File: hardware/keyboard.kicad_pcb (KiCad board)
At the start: 2 copper layers, 64 parts

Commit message: Progress on circuit design
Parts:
- moved CHERRY 350.5 mm to (0.00, 0.00)
- moved CHERRY 148.0 mm to (154.5, 211.2)
- moved CHERRY 117.4 mm to (96.8, -56.9)
- moved CHERRY 117.4 mm to (115.8, -56.6)
- moved CHERRY 117.4 mm to (331.0, 17.0)
- moved CHERRY 117.4 mm to (342.4, -40.1)
- moved CHERRY 117.4 mm to (298.7, -56.9)
- moved CHERRY 117.4 mm to (289.6, -1.02)
- moved CHERRY 117.4 mm to (283.0, -38.1)
- moved CHERRY 117.4 mm to (75.4, -58.4)
- moved CHERRY 117.4 mm to (345.7, -21.6)
- moved CHERRY 117.4 mm to (327.7, -1.52)
- moved CHERRY 117.4 mm to (324.4, -20.1)
- moved CHERRY 117.4 mm to (317.8, -57.1)
- moved CHERRY 117.4 mm to (308.6, -1.27)
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
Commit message: WIP schematic + PCB design
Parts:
- removed CHERRY (x10): MX, keyboard-modules:CHERRY_PCB_125H
- removed CHERRY (x4): MX, keyboard-modules:CHERRY_PCB_150H
- removed CHERRY (x50): MX, keyboard-modules:CHERRY_PCB_100H
- added C1: 18pF, Capacitors_SMD:C_1206_HandSoldering, F.Cu at (273.9, 52.7)
- added C2: 18pF, Capacitors_SMD:C_1206_HandSoldering, F.Cu at (253.1, 58.5)
- added C3: 1uF, Capacitors_SMD:C_1206_HandSoldering, F.Cu at (260.0, 58.5)
- added D1: LED, LEDs:LED_1206, F.Cu at (401.9, 52.6)
- added D10: D_Small, Diodes_SMD:D_1206, F.Cu at (381.9, 58.5)
- added D11: D_Small, Diodes_SMD:D_1206, F.Cu at (183.9, 83.3)
- added D12: D_Small, Diodes_SMD:D_1206, F.Cu at (190.3, 77.6)
- added D13: D_Small, Diodes_SMD:D_1206, F.Cu at (389.4, 52.8)
- added D14: D_Small, Diodes_SMD:D_1206, F.Cu at (203.2, 45.9)
- added D15: D_Small, Diodes_SMD:D_1206, F.Cu at (203.2, 40.2)
- added D16: D_Small, Diodes_SMD:D_1206, F.Cu at (375.5, 58.5)
- added D17: D_Small, Diodes_SMD:D_1206, F.Cu at (369.1, 58.5)
- added D18: D_Small, Diodes_SMD:D_1206, F.Cu at (203.2, 57.4)
- added D19: D_Small, Diodes_SMD:D_1206, F.Cu at (209.6, 51.7)
- added D2: D_Small, Diodes_SMD:D_1206, F.Cu at (196.7, 77.6)
- added D20: D_Small, Diodes_SMD:D_1206, F.Cu at (203.2, 51.7)
- added D21: D_Small, Diodes_SMD:D_1206, F.Cu at (209.6, 45.9)
- added D22: D_Small, Diodes_SMD:D_1206, F.Cu at (349.9, 58.5)
- added D23: D_Small, Diodes_SMD:D_1206, F.Cu at (209.6, 40.2)
- added D24: D_Small, Diodes_SMD:D_1206, F.Cu at (376.6, 52.8)
- added D25: D_Small, Diodes_SMD:D_1206, F.Cu at (209.6, 34.4)
- added D26: D_Small, Diodes_SMD:D_1206, F.Cu at (362.7, 58.5)
- added D27: D_Small, Diodes_SMD:D_1206, F.Cu at (370.2, 52.8)
- added D28: D_Small, Diodes_SMD:D_1206, F.Cu at (363.8, 52.8)
- added D29: D_Small, Diodes_SMD:D_1206, F.Cu at (357.4, 52.8)
- added D3: D_Small, Diodes_SMD:D_1206, F.Cu at (190.3, 83.3)
- added D30: D_Small, Diodes_SMD:D_1206, F.Cu at (356.3, 58.5)
- added D31: D_Small, Diodes_SMD:D_1206, F.Cu at (183.9, 94.8)
- added D32: D_Small, Diodes_SMD:D_1206, F.Cu at (383.0, 52.8)
- added D33: D_Small, Diodes_SMD:D_1206, F.Cu at (183.9, 89.1)
- added D34: D_Small, Diodes_SMD:D_1206, F.Cu at (209.6, 28.7)
- added D35: D_Small, Diodes_SMD:D_1206, F.Cu at (203.2, 28.7)
- added D36: D_Small, Diodes_SMD:D_1206, F.Cu at (209.6, 22.9)
- added D37: D_Small, Diodes_SMD:D_1206, F.Cu at (203.2, 22.9)
- added D38: D_Small, Diodes_SMD:D_1206, F.Cu at (209.6, 17.2)
- added D39: D_Small, Diodes_SMD:D_1206, F.Cu at (343.5, 58.5)
- added D4: D_Small, Diodes_SMD:D_1206, F.Cu at (388.3, 58.5)
- added D40: D_Small, Diodes_SMD:D_1206, F.Cu at (319.0, 52.8)
- added D41: D_Small, Diodes_SMD:D_1206, F.Cu at (337.1, 58.5)
- added D42: D_Small, Diodes_SMD:D_1206, F.Cu at (203.2, 34.4)
- added D43: D_Small, Diodes_SMD:D_1206, F.Cu at (344.6, 52.8)
- added D44: D_Small, Diodes_SMD:D_1206, F.Cu at (203.2, 17.2)
- added D45: D_Small, Diodes_SMD:D_1206, F.Cu at (338.2, 52.8)
- added D46: D_Small, Diodes_SMD:D_1206, F.Cu at (330.7, 58.5)
- added D47: D_Small, Diodes_SMD:D_1206, F.Cu at (324.3, 58.5)
- added D48: D_Small, Diodes_SMD:D_1206, F.Cu at (331.8, 52.8)
- added D49: D_Small, Diodes_SMD:D_1206, F.Cu at (325.4, 52.8)
- added D5: D_Small, Diodes_SMD:D_1206, F.Cu at (203.2, 68.9)
- added D50: D_Small, Diodes_SMD:D_1206, F.Cu at (285.9, 58.5)
- added D51: D_Small, Diodes_SMD:D_1206, F.Cu at (317.9, 58.5)
- added D52: D_Small, Diodes_SMD:D_1206, F.Cu at (311.5, 58.5)
- added D53: D_Small, Diodes_SMD:D_1206, F.Cu at (305.1, 58.5)
- added D54: D_Small, Diodes_SMD:D_1206, F.Cu at (312.6, 52.8)
- added D55: D_Small, Diodes_SMD:D_1206, F.Cu at (306.2, 52.8)
- added D56: D_Small, Diodes_SMD:D_1206, F.Cu at (299.8, 52.8)
- added D57: D_Small, Diodes_SMD:D_1206, F.Cu at (298.7, 58.5)
- added D58: D_Small, Diodes_SMD:D_1206, F.Cu at (292.3, 58.5)
- added D59: D_Small, Diodes_SMD:D_1206, F.Cu at (183.9, 77.6)
- added D6: D_Small, Diodes_SMD:D_1206, F.Cu at (209.6, 63.2)
- added D60: D_Small, Diodes_SMD:D_1206, F.Cu at (293.4, 52.8)
- added D61: D_Small, Diodes_SMD:D_1206, F.Cu at (287.0, 52.8)
- added D62: D_Small, Diodes_SMD:D_1206, F.Cu at (280.6, 52.8)
- added D63: D_Small, Diodes_SMD:D_1206, F.Cu at (279.5, 58.6)
- added D64: D_Small, Diodes_SMD:D_1206, F.Cu at (273.1, 58.6)
- added D65: D_Small, Diodes_SMD:D_1206, F.Cu at (266.7, 58.6)
- added D66: D_Small, Diodes_SMD:D_1206, F.Cu at (351.0, 52.8)
- added D7: D_Small, Diodes_SMD:D_1206, F.Cu at (395.8, 52.8)
- added D8: D_Small, Diodes_SMD:D_1206, F.Cu at (203.2, 63.2)
- added D9: D_Small, Diodes_SMD:D_1206, F.Cu at (209.6, 57.4)
- added F1: Polyfuse_Small, Fuse_Holders_and_Fuses:Fuse_SMD1206_HandSoldering, F.Cu at (234.6, 53.2)
- added J1: USB_OTG, Connectors_USB:USB_Micro-B_Molex-105017-0001, F.Cu at (245.0, 55.0)
- added R1: 1k, Resistors_SMD:R_1206_HandSoldering, F.Cu at (267.0, 52.8)
- added R2: 22, Resistors_SMD:R_1206_HandSoldering, F.Cu at (260.0, 52.8)
- added R3: 22, Resistors_SMD:R_1206_HandSoldering, F.Cu at (253.1, 52.8)
- added S1: SPST, keyboard-modules:CHERRY_PCB_100H, F.Cu at (362.9, 118.5)
- added S10: SPST, keyboard-modules:CHERRY_PCB_100H, F.Cu at (304.9, 118.5)
- added S11: SPST, keyboard-modules:CHERRY_PCB_100H, F.Cu at (324.2, 137.9)
- added S12: SPST, keyboard-modules:CHERRY_PCB_100H, F.Cu at (285.6, 137.9)
- added S13: SPST, keyboard-modules:CHERRY_PCB_100H, F.Cu at (362.9, 176.5)
- added S14: SPST, keyboard-modules:CHERRY_PCB_100H, F.Cu at (141.6, 120.0)
- added S15: SPST, keyboard-modules:CHERRY_PCB_100H, F.Cu at (266.2, 176.5)
- added S16: SPST, keyboard-modules:CHERRY_PCB_100H, F.Cu at (186.2, 214.8)
- added S17: SPST, keyboard-modules:CHERRY_PCB_100H, F.Cu at (285.6, 118.5)
- added S18: SPST, keyboard-modules:CHERRY_PCB_100H, F.Cu at (304.9, 137.9)
- added S19: SPST, keyboard-modules:CHERRY_PCB_100H, F.Cu at (324.2, 157.2)
- added S2: SPST, keyboard-modules:CHERRY_PCB_100H, F.Cu at (244.2, 214.8)
- added S20: SPST, keyboard-modules:CHERRY_PCB_100H, F.Cu at (343.6, 176.5)
- added S21: SPST, keyboard-modules:CHERRY_PCB_100H, F.Cu at (362.9, 195.9)
- added S22: SPST, keyboard-modules:CHERRY_PCB_100H, F.Cu at (266.2, 118.5)
- added S23: SPST, keyboard-modules:CHERRY_PCB_100H, F.Cu at (64.3, 139.3)
- added S24: SPST, keyboard-modules:CHERRY_PCB_100H, F.Cu at (304.9, 157.2)
- added S25: SPST, keyboard-modules:CHERRY_PCB_100H, F.Cu at (324.2, 176.5)
- added S26: SPST, keyboard-modules:CHERRY_PCB_100H, F.Cu at (343.6, 195.9)
- added S27: SPST, keyboard-modules:CHERRY_PCB_100H, F.Cu at (161.0, 120.0)
- added S28: SPST, keyboard-modules:CHERRY_PCB_100H, F.Cu at (266.2, 137.9)
- added S29: SPST, keyboard-modules:CHERRY_PCB_100H, F.Cu at (285.6, 157.2)
- added S3: SPST, keyboard-modules:CHERRY_PCB_100H, F.Cu at (362.9, 137.9)
- added S30: SPST, keyboard-modules:CHERRY_PCB_100H, F.Cu at (304.9, 176.5)
- added S31: SPST, keyboard-modules:CHERRY_PCB_100H, F.Cu at (324.2, 195.9)
- added S32: SPST, keyboard-modules:CHERRY_PCB_100H, F.Cu at (324.2, 118.5)
- added S33: SPST, keyboard-modules:CHERRY_PCB_100H, F.Cu at (266.2, 157.2)
- added S34: SPST, keyboard-modules:CHERRY_PCB_100H, F.Cu at (285.6, 176.5)
- added S35: SPST, keyboard-modules:CHERRY_PCB_100H, F.Cu at (304.9, 195.9)
- added S36: SPST, keyboard-modules:CHERRY_PCB_100H, F.Cu at (122.3, 120.0)
- added S37: SPST, keyboard-modules:CHERRY_PCB_100H, F.Cu at (141.6, 139.3)
- added S38: SPST, keyboard-modules:CHERRY_PCB_100H, F.Cu at (161.0, 158.7)
- added S39: SPST, keyboard-modules:CHERRY_PCB_100H, F.Cu at (122.3, 158.7)
- added S4: SPST, keyboard-modules:CHERRY_PCB_100H, F.Cu at (343.6, 118.5)
- added S40: SPST, keyboard-modules:CHERRY_PCB_100H, F.Cu at (285.6, 195.9)
- added S41: SPST, keyboard-modules:CHERRY_PCB_100H, F.Cu at (161.0, 139.3)
- added S42: SPST, keyboard-modules:CHERRY_PCB_100H, F.Cu at (103.0, 120.0)
- added S43: SPST, keyboard-modules:CHERRY_PCB_100H, F.Cu at (122.3, 139.3)
- added S44: SPST, keyboard-modules:CHERRY_PCB_100H, F.Cu at (141.6, 158.7)
- added S45: SPST, keyboard-modules:CHERRY_PCB_100H, F.Cu at (161.0, 178.0)
- added S46: SPST, keyboard-modules:CHERRY_PCB_100H, F.Cu at (266.2, 195.9)
- added S47: SPST, keyboard-modules:CHERRY_PCB_100H, F.Cu at (83.6, 120.0)
- added S48: SPST, keyboard-modules:CHERRY_PCB_100H, F.Cu at (103.0, 139.3)
- added S49: SPST, keyboard-modules:CHERRY_PCB_100H, F.Cu at (103.0, 178.0)
- added S5: SPST, keyboard-modules:CHERRY_PCB_100H, F.Cu at (224.9, 214.8)
- added S50: SPST, keyboard-modules:CHERRY_PCB_100H, F.Cu at (161.0, 197.3)
- added S51: SPST, keyboard-modules:CHERRY_PCB_100H, F.Cu at (64.3, 120.0)
- added S52: SPST, keyboard-modules:CHERRY_PCB_100H, F.Cu at (83.6, 139.3)
- added S53: SPST, keyboard-modules:CHERRY_PCB_100H, F.Cu at (103.0, 158.7)
- added S54: SPST, keyboard-modules:CHERRY_PCB_100H, F.Cu at (122.3, 178.0)
- added S55: SPST, keyboard-modules:CHERRY_PCB_100H, F.Cu at (141.6, 197.3)
- added S56: SPST, keyboard-modules:CHERRY_PCB_100H, F.Cu at (64.3, 197.3)
- added S57: SPST, keyboard-modules:CHERRY_PCB_100H, F.Cu at (83.6, 158.7)
- added S58: SPST, keyboard-modules:CHERRY_PCB_100H, F.Cu at (141.6, 178.0)
- added S59: SPST, keyboard-modules:CHERRY_PCB_100H, F.Cu at (122.3, 197.3)
- added S6: SPST, keyboard-modules:CHERRY_PCB_100H, F.Cu at (343.6, 157.2)
- added S60: SPST, keyboard-modules:CHERRY_PCB_100H, F.Cu at (64.3, 158.7)
- added S61: SPST, keyboard-modules:CHERRY_PCB_100H, F.Cu at (83.6, 178.0)
- added S62: SPST, keyboard-modules:CHERRY_PCB_100H, F.Cu at (103.0, 197.3)
- added S63: SPST, keyboard-modules:CHERRY_PCB_100H, F.Cu at (64.3, 178.0)
- added S64: SPST, keyboard-modules:CHERRY_PCB_100H, F.Cu at (83.6, 197.3)
- added S7: SPST, keyboard-modules:CHERRY_PCB_100H, F.Cu at (343.6, 137.9)
- added S8: SPST, keyboard-modules:CHERRY_PCB_100H, F.Cu at (362.9, 157.2)
- added S9: SPST, keyboard-modules:CHERRY_PCB_100H, F.Cu at (205.5, 214.8)
- added U1: ATMEGA32U4-AU, Housings_QFP:TQFP-44_10x10mm_Pitch0.8mm, F.Cu at (207.0, 5.88)
- added Y1: 16MHz, Crystals:Crystal_SMD_2012-2pin_2.0x1.2mm_HandSoldering, F.Cu at (394.1, 58.5)

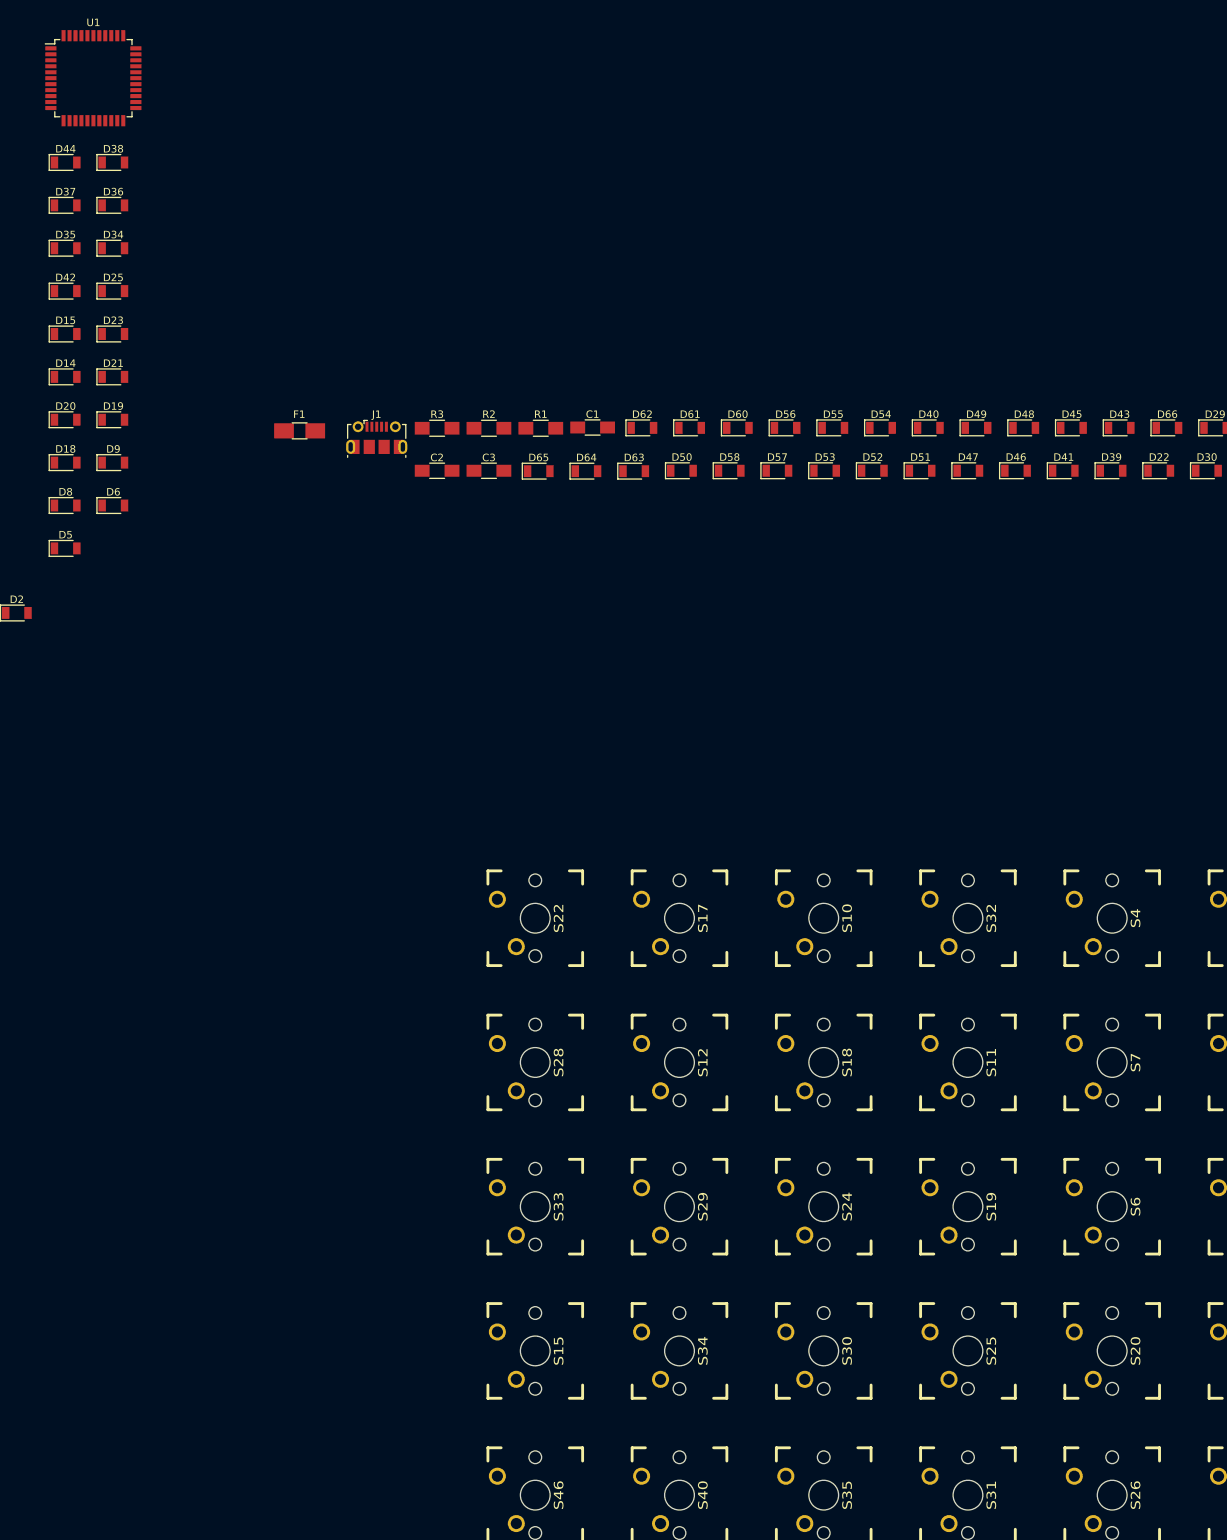
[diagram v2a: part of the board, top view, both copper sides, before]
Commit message: Extract keys into sheets, add MCP23018
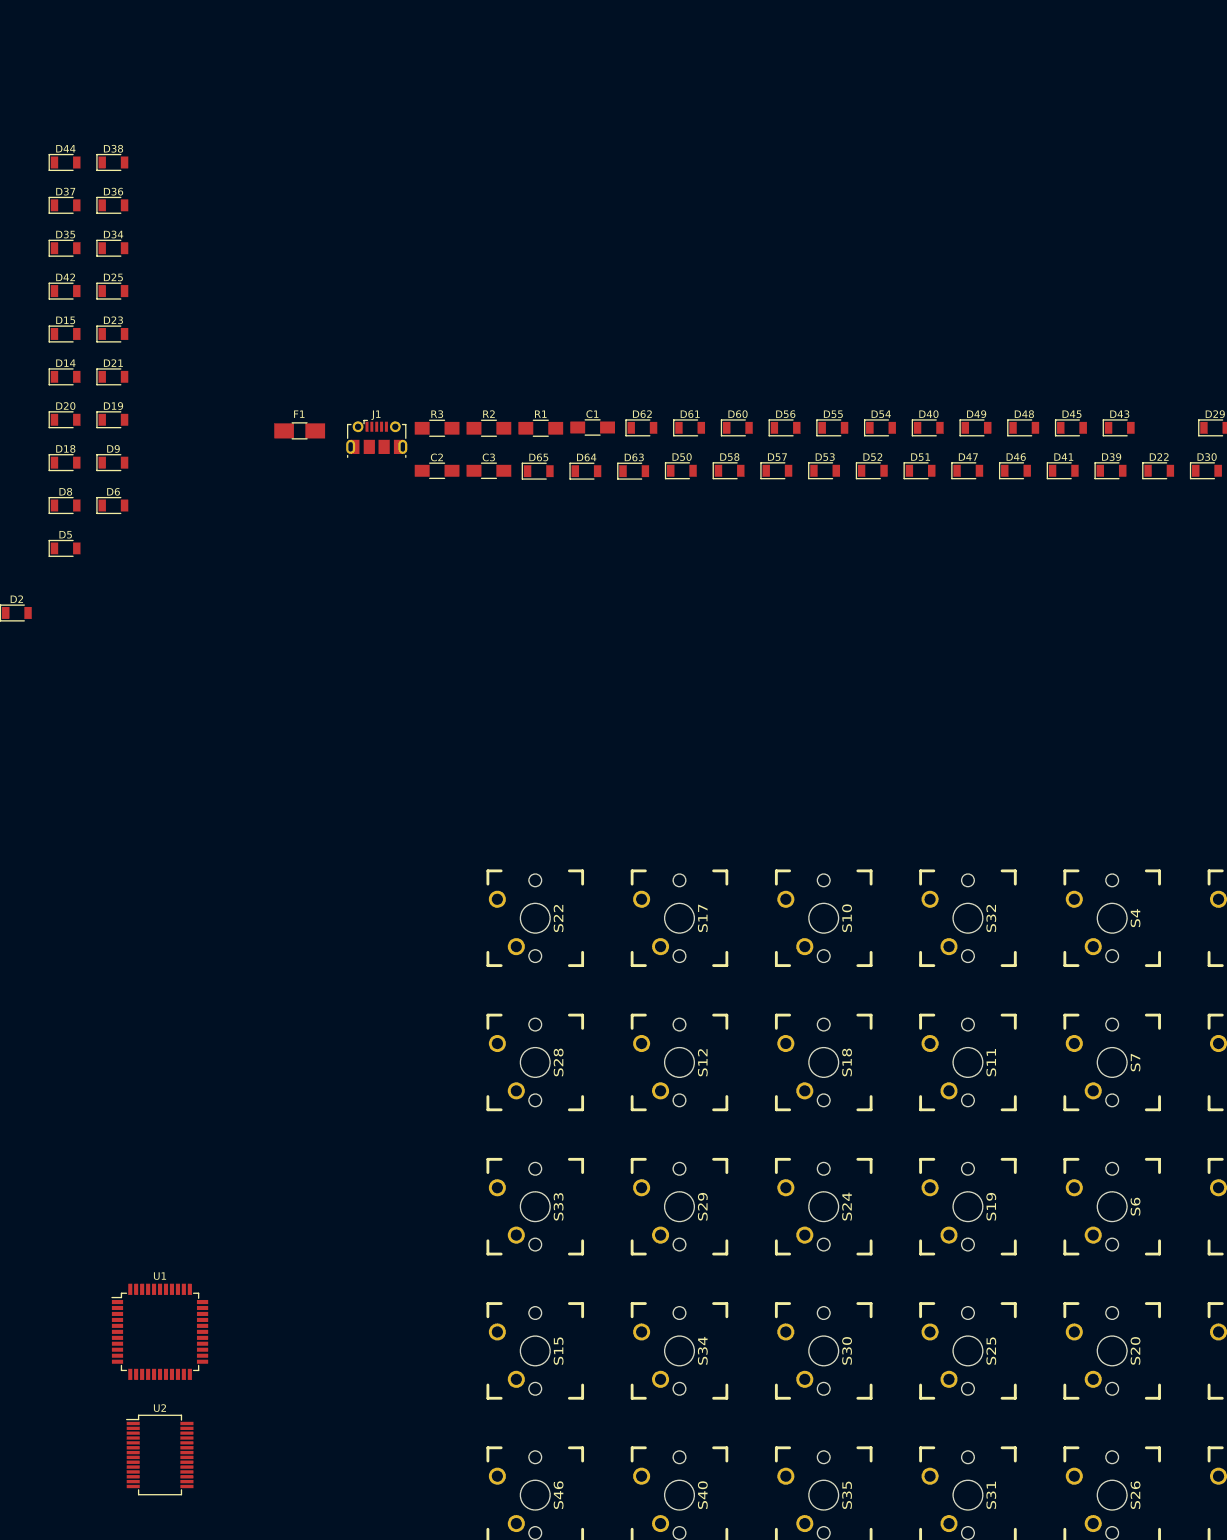
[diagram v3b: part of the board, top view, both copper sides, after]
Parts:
- removed D66: D_Small, Diodes_SMD:D_1206
- added U2: MCP23018_SSOP, Housings_SSOP:SSOP-28_5.3x10.2mm_Pitch0.65mm, F.Cu at (215.9, 190.5)
- R1: value 1k -> 22
- R3: value 22 -> 1k
- moved U1 168.3 mm to (215.9, 174.0)
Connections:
- D10 pad 1: /COL7 -> COL1
- D10 pad 2: (no net) -> Net-(D10-Pad2)
- D11 pad 1: /COL8 -> COL1
- D11 pad 2: (no net) -> Net-(D11-Pad2)
- D12 pad 1: /COL9 -> COL2
- D12 pad 2: (no net) -> Net-(D12-Pad2)
- D13 pad 1: /COL10 -> COL2
- D13 pad 2: (no net) -> Net-(D13-Pad2)
- D14 pad 1: /COL11 -> COL2
- D14 pad 2: (no net) -> Net-(D14-Pad2)
- D15 pad 1: /COL12 -> COL2
- D15 pad 2: (no net) -> Net-(D15-Pad2)
- D16 pad 1: /COL0 -> COL2
- D16 pad 2: (no net) -> Net-(D16-Pad2)
- D17 pad 1: /COL1 -> COL3
- D17 pad 2: (no net) -> Net-(D17-Pad2)
- D18 pad 1: /COL2 -> COL3
- D18 pad 2: (no net) -> Net-(D18-Pad2)
- D19 pad 1: /COL3 -> COL3
- D19 pad 2: (no net) -> Net-(D19-Pad2)
- D2 pad 1: (no net) -> COL0
- D2 pad 2: (no net) -> Net-(D2-Pad2)
- D20 pad 1: /COL4 -> COL3
- D20 pad 2: (no net) -> Net-(D20-Pad2)
- D21 pad 1: /COL5 -> COL3
- D21 pad 2: (no net) -> Net-(D21-Pad2)
- D22 pad 1: /COL6 -> COL4
- D22 pad 2: (no net) -> Net-(D22-Pad2)
- D23 pad 1: /COL7 -> COL4
- D23 pad 2: (no net) -> Net-(D23-Pad2)
- D24 pad 1: /COL8 -> COL4
- D24 pad 2: (no net) -> Net-(D24-Pad2)
- D25 pad 1: /COL9 -> COL4
- D25 pad 2: (no net) -> Net-(D25-Pad2)
- D26 pad 1: /COL10 -> COL4
- D26 pad 2: (no net) -> Net-(D26-Pad2)
- D27 pad 1: /COL11 -> COL5
- D27 pad 2: (no net) -> Net-(D27-Pad2)
- D28 pad 1: /COL12 -> COL5
- D28 pad 2: (no net) -> Net-(D28-Pad2)
- D29 pad 1: /COL0 -> COL5
- D29 pad 2: (no net) -> Net-(D29-Pad2)
- D3 pad 1: /COL0 -> COL0
- D3 pad 2: (no net) -> Net-(D3-Pad2)
- D30 pad 1: /COL1 -> COL5
- D30 pad 2: (no net) -> Net-(D30-Pad2)
- D31 pad 1: /COL2 -> COL5
- D31 pad 2: (no net) -> Net-(D31-Pad2)
- D32 pad 1: /COL3 -> COL6
- D32 pad 2: (no net) -> Net-(D32-Pad2)
- D33 pad 1: /COL4 -> COL6
- D33 pad 2: (no net) -> Net-(D33-Pad2)
- D34 pad 1: /COL5 -> COL6
- D34 pad 2: (no net) -> Net-(D34-Pad2)
- D35 pad 1: /COL6 -> COL6
- D35 pad 2: (no net) -> Net-(D35-Pad2)
- D36 pad 1: /COL7 -> COL6
- D36 pad 2: (no net) -> Net-(D36-Pad2)
- D37 pad 1: /COL8 -> COL7
- D37 pad 2: (no net) -> Net-(D37-Pad2)
- D38 pad 1: /COL9 -> COL7
- D38 pad 2: (no net) -> Net-(D38-Pad2)
- D39 pad 1: /COL10 -> COL7
- D39 pad 2: (no net) -> Net-(D39-Pad2)
- D4 pad 1: /COL1 -> COL0
- D4 pad 2: (no net) -> Net-(D4-Pad2)
- D40 pad 1: /COL11 -> COL7
- D40 pad 2: (no net) -> Net-(D40-Pad2)
- D41 pad 1: /COL12 -> COL7
- D41 pad 2: (no net) -> Net-(D41-Pad2)
- D42 pad 1: /COL0 -> COL8
- D42 pad 2: (no net) -> Net-(D42-Pad2)
- D43 pad 1: /COL1 -> COL8
- D43 pad 2: (no net) -> Net-(D43-Pad2)
- D44 pad 1: /COL2 -> COL8
- D44 pad 2: (no net) -> Net-(D44-Pad2)
- D45 pad 1: /COL3 -> COL8
- D45 pad 2: (no net) -> Net-(D45-Pad2)
- D46 pad 1: /COL4 -> COL8
- D46 pad 2: (no net) -> Net-(D46-Pad2)
- D47 pad 1: /COL5 -> COL9
- D47 pad 2: (no net) -> Net-(D47-Pad2)
- D48 pad 1: /COL6 -> COL9
- D48 pad 2: (no net) -> Net-(D48-Pad2)
- D49 pad 1: /COL7 -> COL9
- D49 pad 2: (no net) -> Net-(D49-Pad2)
- D5 pad 1: /COL2 -> COL0
- D5 pad 2: (no net) -> Net-(D5-Pad2)
- D50 pad 1: /COL8 -> COL9
- D50 pad 2: (no net) -> Net-(D50-Pad2)
- D51 pad 1: /COL9 -> COL9
- D51 pad 2: (no net) -> Net-(D51-Pad2)
- D52 pad 1: /COL10 -> COL10
- D52 pad 2: (no net) -> Net-(D52-Pad2)
- D53 pad 1: /COL11 -> COL10
- D53 pad 2: (no net) -> Net-(D53-Pad2)
- D54 pad 1: /COL12 -> COL10
- D54 pad 2: (no net) -> Net-(D54-Pad2)
- D55 pad 1: /COL0 -> COL10
- D55 pad 2: (no net) -> Net-(D55-Pad2)
- D56 pad 1: /COL1 -> COL10
- D56 pad 2: (no net) -> Net-(D56-Pad2)
- D57 pad 1: /COL2 -> COL11
- D57 pad 2: (no net) -> Net-(D57-Pad2)
- D58 pad 1: /COL3 -> COL11
- D58 pad 2: (no net) -> Net-(D58-Pad2)
- D59 pad 1: /COL4 -> COL11
- D59 pad 2: (no net) -> Net-(D59-Pad2)
- D6 pad 1: /COL3 -> COL0
- D6 pad 2: (no net) -> Net-(D6-Pad2)
- D60 pad 1: /COL5 -> COL11
- D60 pad 2: (no net) -> Net-(D60-Pad2)
- D61 pad 1: /COL6 -> COL11
- D61 pad 2: (no net) -> Net-(D61-Pad2)
- D62 pad 1: /COL7 -> COL12
- D62 pad 2: (no net) -> Net-(D62-Pad2)
- D63 pad 1: /COL8 -> COL12
- D63 pad 2: (no net) -> Net-(D63-Pad2)
- D64 pad 1: /COL9 -> COL12
- D64 pad 2: (no net) -> Net-(D64-Pad2)
- D65 pad 1: /COL10 -> COL12
- D65 pad 2: (no net) -> Net-(D65-Pad2)
- D7 pad 1: /COL4 -> COL1
- D7 pad 2: (no net) -> Net-(D7-Pad2)
- D8 pad 1: /COL5 -> COL1
- D8 pad 2: (no net) -> Net-(D8-Pad2)
- D9 pad 1: /COL6 -> COL1
- D9 pad 2: (no net) -> Net-(D9-Pad2)
- R1 pad 1: +5V -> Net-(R1-Pad1)
- R1 pad 2: Net-(D1-Pad2) -> Net-(J1-Pad3)
- R2 pad 2: Net-(J1-Pad3) -> Net-(J1-Pad2)
- R3 pad 1: Net-(R3-Pad1) -> +5V
- R3 pad 2: Net-(J1-Pad2) -> Net-(D1-Pad2)
- S1 pad 1: (no net) -> ROW0
- S1 pad 2: (no net) -> Net-(D2-Pad2)
- S10 pad 1: (no net) -> /K10/ROW
- S10 pad 2: (no net) -> Net-(D11-Pad2)
- S11 pad 1: (no net) -> ROW0
- S11 pad 2: (no net) -> Net-(D12-Pad2)
- S12 pad 1: (no net) -> ROW1
- S12 pad 2: (no net) -> Net-(D13-Pad2)
- S13 pad 1: (no net) -> ROW2
- S13 pad 2: (no net) -> Net-(D14-Pad2)
- S14 pad 1: (no net) -> ROW3
- S14 pad 2: (no net) -> Net-(D15-Pad2)
- S15 pad 1: (no net) -> /K10/ROW
- S15 pad 2: (no net) -> Net-(D16-Pad2)
- S16 pad 1: (no net) -> ROW0
- S16 pad 2: (no net) -> Net-(D17-Pad2)
- S17 pad 1: (no net) -> ROW1
- S17 pad 2: (no net) -> Net-(D18-Pad2)
- S18 pad 1: (no net) -> ROW2
- S18 pad 2: (no net) -> Net-(D19-Pad2)
- S19 pad 1: (no net) -> ROW3
- S19 pad 2: (no net) -> Net-(D20-Pad2)
- S2 pad 1: (no net) -> ROW1
- S2 pad 2: (no net) -> Net-(D3-Pad2)
- S20 pad 1: (no net) -> /K10/ROW
- S20 pad 2: (no net) -> Net-(D21-Pad2)
- S21 pad 1: (no net) -> ROW0
- S21 pad 2: (no net) -> Net-(D22-Pad2)
- S22 pad 1: (no net) -> ROW1
- S22 pad 2: (no net) -> Net-(D23-Pad2)
- S23 pad 1: (no net) -> ROW2
- S23 pad 2: (no net) -> Net-(D24-Pad2)
- S24 pad 1: (no net) -> ROW3
- S24 pad 2: (no net) -> Net-(D25-Pad2)
- S25 pad 1: (no net) -> /K10/ROW
- S25 pad 2: (no net) -> Net-(D26-Pad2)
- S26 pad 1: (no net) -> ROW0
- S26 pad 2: (no net) -> Net-(D27-Pad2)
- S27 pad 1: (no net) -> ROW1
- S27 pad 2: (no net) -> Net-(D28-Pad2)
- S28 pad 1: (no net) -> ROW2
- S28 pad 2: (no net) -> Net-(D29-Pad2)
- S29 pad 1: (no net) -> ROW3
- S29 pad 2: (no net) -> Net-(D30-Pad2)
- S3 pad 1: (no net) -> ROW2
- S3 pad 2: (no net) -> Net-(D4-Pad2)
- S30 pad 1: (no net) -> /K10/ROW
- S30 pad 2: (no net) -> Net-(D31-Pad2)
- S31 pad 1: (no net) -> ROW0
- S31 pad 2: (no net) -> Net-(D32-Pad2)
- S32 pad 1: (no net) -> ROW1
- S32 pad 2: (no net) -> Net-(D33-Pad2)
- S33 pad 1: (no net) -> ROW2
- S33 pad 2: (no net) -> Net-(D34-Pad2)
- S34 pad 1: (no net) -> ROW3
- S34 pad 2: (no net) -> Net-(D35-Pad2)
- S35 pad 1: (no net) -> /K10/ROW
- S35 pad 2: (no net) -> Net-(D36-Pad2)
- S36 pad 1: (no net) -> ROW0
- S36 pad 2: (no net) -> Net-(D37-Pad2)
- S37 pad 1: (no net) -> ROW1
- S37 pad 2: (no net) -> Net-(D38-Pad2)
- S38 pad 1: (no net) -> ROW2
- S38 pad 2: (no net) -> Net-(D39-Pad2)
- S39 pad 1: (no net) -> ROW3
- S39 pad 2: (no net) -> Net-(D40-Pad2)
- S4 pad 1: (no net) -> ROW3
- S4 pad 2: (no net) -> Net-(D5-Pad2)
- S40 pad 1: (no net) -> /K10/ROW
- S40 pad 2: (no net) -> Net-(D41-Pad2)
- S41 pad 1: (no net) -> ROW0
- S41 pad 2: (no net) -> Net-(D42-Pad2)
- S42 pad 1: (no net) -> ROW1
- S42 pad 2: (no net) -> Net-(D43-Pad2)
- S43 pad 1: (no net) -> ROW2
- S43 pad 2: (no net) -> Net-(D44-Pad2)
- S44 pad 1: (no net) -> ROW3
- S44 pad 2: (no net) -> Net-(D45-Pad2)
- S45 pad 1: (no net) -> /K10/ROW
- S45 pad 2: (no net) -> Net-(D46-Pad2)
- S46 pad 1: (no net) -> ROW0
- S46 pad 2: (no net) -> Net-(D47-Pad2)
- S47 pad 1: (no net) -> ROW1
- S47 pad 2: (no net) -> Net-(D48-Pad2)
- S48 pad 1: (no net) -> ROW2
- S48 pad 2: (no net) -> Net-(D49-Pad2)
- S49 pad 1: (no net) -> ROW3
- S49 pad 2: (no net) -> Net-(D50-Pad2)
- S5 pad 1: (no net) -> /K10/ROW
- S5 pad 2: (no net) -> Net-(D6-Pad2)
- S50 pad 1: (no net) -> /K10/ROW
- S50 pad 2: (no net) -> Net-(D51-Pad2)
- S51 pad 1: (no net) -> ROW0
- S51 pad 2: (no net) -> Net-(D52-Pad2)
- S52 pad 1: (no net) -> ROW1
- S52 pad 2: (no net) -> Net-(D53-Pad2)
- S53 pad 1: (no net) -> ROW2
- S53 pad 2: (no net) -> Net-(D54-Pad2)
- S54 pad 1: (no net) -> ROW3
- S54 pad 2: (no net) -> Net-(D55-Pad2)
- S55 pad 1: (no net) -> /K10/ROW
- S55 pad 2: (no net) -> Net-(D56-Pad2)
- S56 pad 1: (no net) -> ROW0
- S56 pad 2: (no net) -> Net-(D57-Pad2)
- S57 pad 1: (no net) -> ROW1
- S57 pad 2: (no net) -> Net-(D58-Pad2)
- S58 pad 1: (no net) -> ROW2
- S58 pad 2: (no net) -> Net-(D59-Pad2)
- S59 pad 1: (no net) -> ROW3
- S59 pad 2: (no net) -> Net-(D60-Pad2)
- S6 pad 1: (no net) -> ROW0
- S6 pad 2: (no net) -> Net-(D7-Pad2)
- S60 pad 1: (no net) -> /K10/ROW
- S60 pad 2: (no net) -> Net-(D61-Pad2)
- S61 pad 1: (no net) -> ROW0
- S61 pad 2: (no net) -> Net-(D62-Pad2)
- S62 pad 1: (no net) -> ROW1
- S62 pad 2: (no net) -> Net-(D63-Pad2)
- S63 pad 1: (no net) -> ROW2
- S63 pad 2: (no net) -> Net-(D64-Pad2)
- S64 pad 1: (no net) -> ROW3
- S64 pad 2: (no net) -> Net-(D65-Pad2)
- S7 pad 1: (no net) -> ROW1
- S7 pad 2: (no net) -> Net-(D8-Pad2)
- S8 pad 1: (no net) -> ROW2
- S8 pad 2: (no net) -> Net-(D9-Pad2)
- S9 pad 1: (no net) -> ROW3
- S9 pad 2: (no net) -> Net-(D10-Pad2)
- U1 pad 10: (no net) -> ROW2
- U1 pad 11: (no net) -> ROW3
- U1 pad 12: /COL2 -> (no net)
- U1 pad 18: /COL5 -> /SCL
- U1 pad 19: /COL6 -> /SDA
- U1 pad 20: /COL7 -> (no net)
- U1 pad 21: /COL8 -> (no net)
- U1 pad 22: /COL10 -> (no net)
- U1 pad 25: /COL9 -> (no net)
- U1 pad 26: /COL11 -> (no net)
- U1 pad 27: /COL12 -> (no net)
- U1 pad 29: /COL0 -> (no net)
- U1 pad 3: Net-(R3-Pad1) -> Net-(R2-Pad1)
- U1 pad 30: /COL1 -> (no net)
- U1 pad 31: /COL3 -> (no net)
- U1 pad 32: /COL4 -> (no net)
- U1 pad 4: Net-(R2-Pad1) -> Net-(R1-Pad1)
- U1 pad 8: (no net) -> ROW0
- U1 pad 9: (no net) -> ROW1
